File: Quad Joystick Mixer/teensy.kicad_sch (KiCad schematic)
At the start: 15 parts, among them SW5 Cherry MX, U20 Teensy4.0

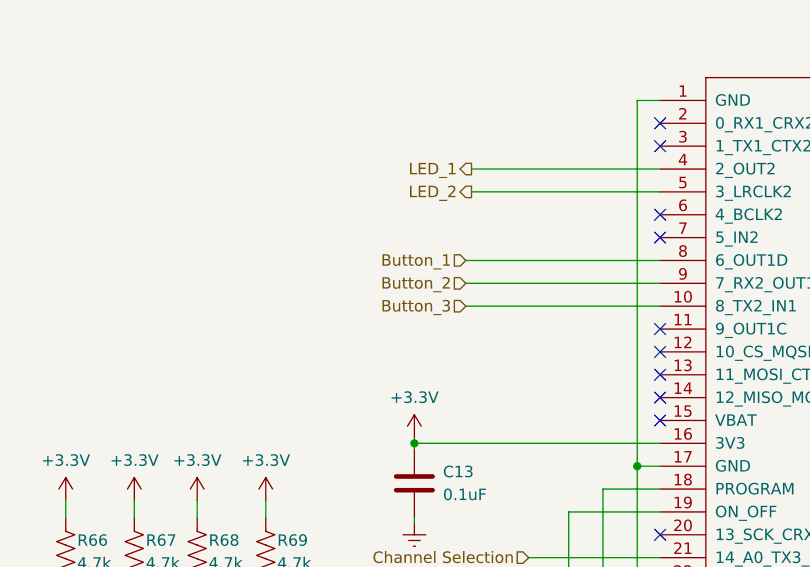
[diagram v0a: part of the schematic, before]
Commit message: changed power supply design and everything re routed
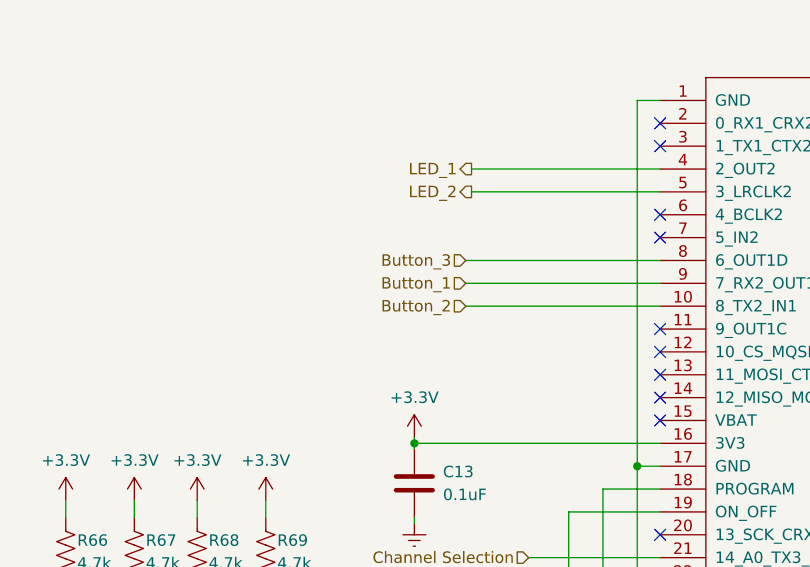
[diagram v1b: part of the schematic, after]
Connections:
- net Button_1: now also U20.9 (7_RX2_OUT1A); no longer U20.8 (6_OUT1D)
- net Button_2: now also U20.10 (8_TX2_IN1); no longer U20.9 (7_RX2_OUT1A)
- net Button_3: now also U20.8 (6_OUT1D); no longer U20.10 (8_TX2_IN1)
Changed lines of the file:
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@@
     (stroke (width 0) (type default))
   )
-  (wire (pts (xy 159.385 121.285) (xy 180.975 121.285))
-    (stroke (width 0) (type default))
-  )
   (wire (pts (xy 180.975 141.605) (xy 174.625 141.605))
     (stroke (width 0) (type default))
@@
     (stroke (width 0) (type default))
   )
-  (wire (pts (xy 159.385 116.205) (xy 180.975 116.205))
-    (stroke (width 0) (type default))
-  )
-  (wire (pts (xy 159.385 118.745) (xy 180.975 118.745))
-    (stroke (width 0) (type default))
-  )
   (wire (pts (xy 243.205 159.385) (xy 243.205 172.72))
     (stroke (width 0) (type default))
@@
     (stroke (width 0) (type default))
   )
+  (wire (pts (xy 159.385 121.285) (xy 180.975 121.285))
+    (stroke (width 0) (type default))
+  )
   (wire (pts (xy 248.285 156.845) (xy 248.285 162.56))
     (stroke (width 0) (type default))
@@
     (stroke (width 0) (type default))
   )
+  (wire (pts (xy 159.385 118.745) (xy 180.975 118.745))
+    (stroke (width 0) (type default))
+  )
   (wire (pts (xy 141.605 190.5) (xy 141.605 192.405))
     (stroke (width 0) (type default))
@@
     (stroke (width 0) (type default))
   )
+  (wire (pts (xy 159.385 116.205) (xy 180.975 116.205))
+    (stroke (width 0) (type default))
+  )
   (wire (pts (xy 178.435 98.425) (xy 178.435 139.065))
     (stroke (width 0) (type default))
@@
     (effects (font (size 1.27 1.27)) (justify right))
   )
-  (hierarchical_label "Button_3" (shape input) (at 159.385 121.285 180) (fields_autoplaced)
+  (hierarchical_label "Button_3" (shape input) (at 159.385 116.205 180) (fields_autoplaced)
     (effects (font (size 1.27 1.27)) (justify right))
   )
@@
     (effects (font (size 1.27 1.27)) (justify right))
   )
-  (hierarchical_label "Button_2" (shape input) (at 159.385 118.745 180) (fields_autoplaced)
+  (hierarchical_label "Button_2" (shape input) (at 159.385 121.285 180) (fields_autoplaced)
     (effects (font (size 1.27 1.27)) (justify right))
   )
@@
     (effects (font (size 1.27 1.27)) (justify right))
   )
-  (hierarchical_label "Button_1" (shape input) (at 159.385 116.205 180) (fields_autoplaced)
+  (hierarchical_label "Button_1" (shape input) (at 159.385 118.745 180) (fields_autoplaced)
     (effects (font (size 1.27 1.27)) (justify right))
   )
